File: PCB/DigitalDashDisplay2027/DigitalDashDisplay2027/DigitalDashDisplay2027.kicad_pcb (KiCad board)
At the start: 2 copper layers, 100 x 56.3 mm, 13 parts, among them IC1 LMR51430YDDCR, J1 Adafruit CAN Pal, J2 53375-0810, U1 Teensy4.0

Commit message: Began restructuring dash PCB, migrated footprints & symbols to the central library
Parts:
- removed J1: Adafruit CAN Pal, CFR 2025 Digital Dash Lib:1X07_ROUND_70
- C6: moved to F.Cu
- moved J2 13.2 mm to (175.9, 109.0)
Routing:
- net /CanLo: track 50.7 -> 0.00 mm
- net /CanHi: track 43.1 -> 0.00 mm
- net +BATT: track 16.9 -> 14.1 mm

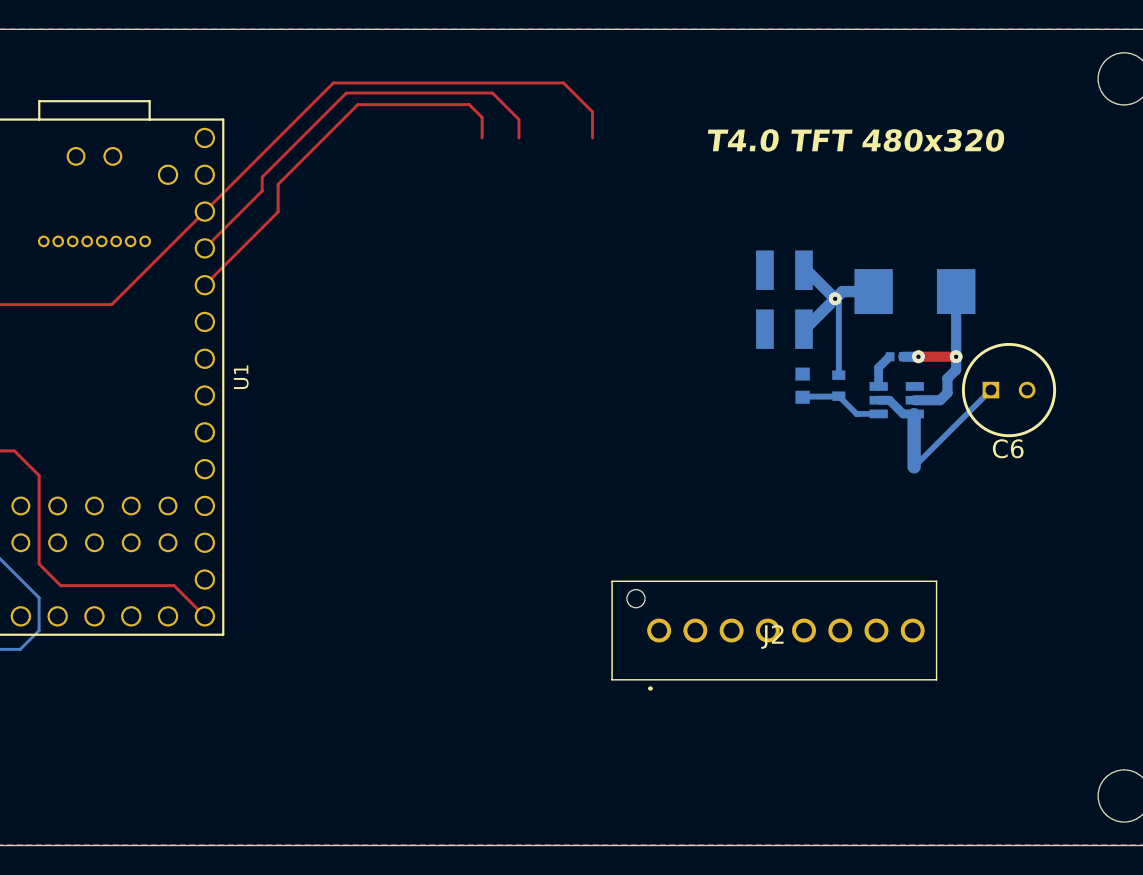
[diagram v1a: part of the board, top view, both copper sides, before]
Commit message: Began redesigning dashboard, changed multi-power rail to single power rail, rerouted buck converter
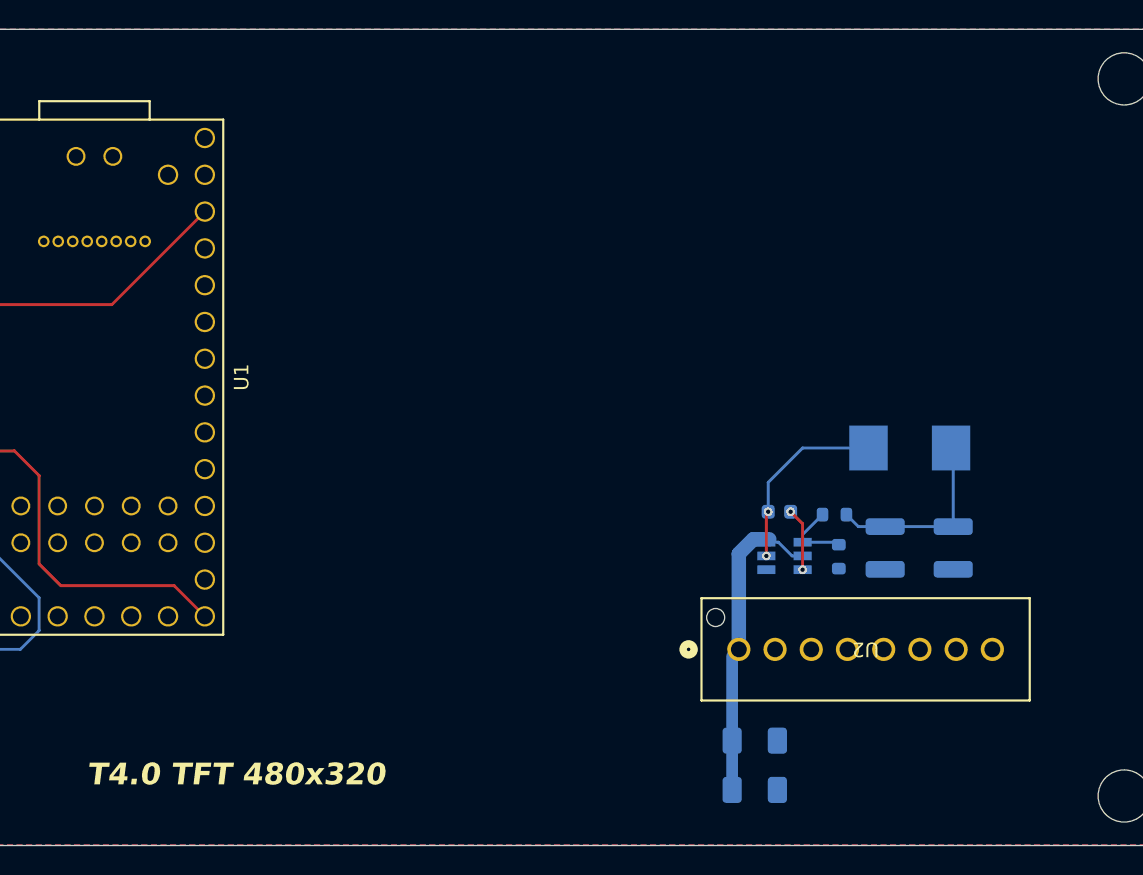
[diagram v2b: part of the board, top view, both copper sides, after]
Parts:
- removed C6: RPA0609101M025B, buck_footprints:CAPPRD250W55D630H1050
- removed C7, C8: CL32A226KOJNNNE, buck_footprints:CAPC3225X270N
- removed IC1: LMR51430YDDCR, buck_footprints:SOT95P280X110-6N
- removed J2: 53375-0810, SamacSys_Parts:533750810
- removed L5: PA4341.682ANLT, buck_footprints:INDPM7166X300N
- removed R6: ERA-3AED104V, buck_footprints:ERA3AEB101V
- removed R7: ERJ-3EKF1372V, buck_footprints:RESC1608X55N
- added C1: CC0603KRX7R7BB104, Capacitor_SMD:C_0603_1608Metric, B.Cu at (184.2, 100.8)
- added C2: C3216X5R1E476M160AC, Capacitor_SMD:C_1206_3216Metric_Pad1.33x1.80mm_HandSolder, B.Cu at (182.5, 120.0)
- added C3: CL32A226KOJNNNE, Capacitor_SMD:C_1210_3225Metric, B.Cu at (191.5, 103.3)
- added C4: CL32A226KOJNNNE, Capacitor_SMD:C_1210_3225Metric, B.Cu at (196.2, 103.3)
- added IC2: LMR51430YDDCR, CFR Library:SOT95P280X110-6N, B.Cu at (184.6, 103.8)
- added L1: PA4341.682ANLT, CFR Library:INDPM7166X300N, B.Cu at (193.2, 96.4)
- added R1: ERA-3AED104V, Resistor_SMD:R_0603_1608Metric, B.Cu at (188.0, 101.0)
- added R2: ERJ-3EKF1372V, Resistor_SMD:R_0603_1608Metric, B.Cu at (188.3, 103.9)
- added U2: ~, CFR Library:CONN08_533750810_MOL, F.Cu at (181.4, 110.3)
- C5: value CL05B104KO5NNNC -> C3216X5R1E476M160AC; footprint buck_footprints:CAPC1005X55N -> Capacitor_SMD:C_1206_3216Metric_Pad1.33x1.80mm_HandSolder
- moved C5 28.3 mm to (182.5, 116.6), turned to 180 degrees
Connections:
- C5 pad 1: Net-(IC1-CB) -> GNDREF
- C5 pad 2: Net-(IC1-SW) -> +BATT
- U1 pad 21: Net-(U1-14_A0_TX3_SPDIF_OUT) -> unconnected-(U1-14_A0_TX3_SPDIF_OUT-Pad21)
- U1 pad 22: Net-(U1-15_A1_RX3_SPDIF_IN) -> unconnected-(U1-15_A1_RX3_SPDIF_IN-Pad22)
- U1 pad 25: Net-(U1-18_A4_SDA0) -> unconnected-(U1-18_A4_SDA0-Pad25)
- U1 pad 26: Net-(U1-19_A5_SCL0) -> unconnected-(U1-19_A5_SCL0-Pad26)
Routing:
- net +3.3V: track 93.5 -> 60.5 mm
- net /CRX: track 28.8 -> 0.08 mm
- net /CTX: track 27.2 -> 0.00 mm
- net Net-(IC1-SW): track 13.4 -> 0.00 mm, vias 2 -> 0
- net Net-(IC2-SW): track 0.00 -> 13.0 mm, vias 0 -> 2
- net +BATT: track 14.1 -> 21.9 mm
- net Net-(IC1-FB): track 5.77 -> 0.00 mm
- net Net-(IC2-FB): track 0.00 -> 5.04 mm
- net Net-(IC2-CB): track 0.00 -> 4.34 mm, vias 0 -> 2
- net Net-(IC1-CB): track 2.41 -> 0.00 mm
- net +5V: track 14.2 -> 13.2 mm, vias 1 -> 0
- added copper zone on F.Cu, net GNDREF
- removed copper zone on F.Cu, net +5V
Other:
- board text added: "Buck traces need to be properly sized"

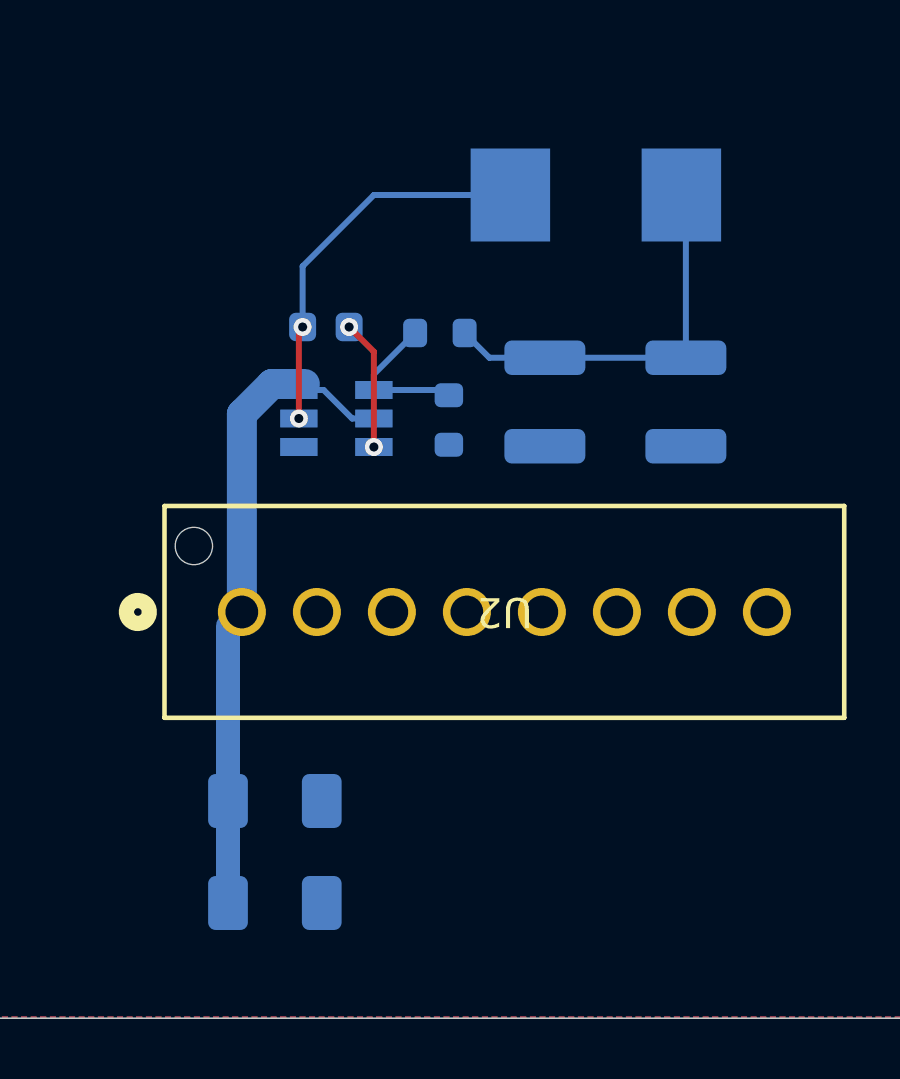
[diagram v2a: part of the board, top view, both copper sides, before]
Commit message: Sized buck converter traces, began re-routing DAQ board
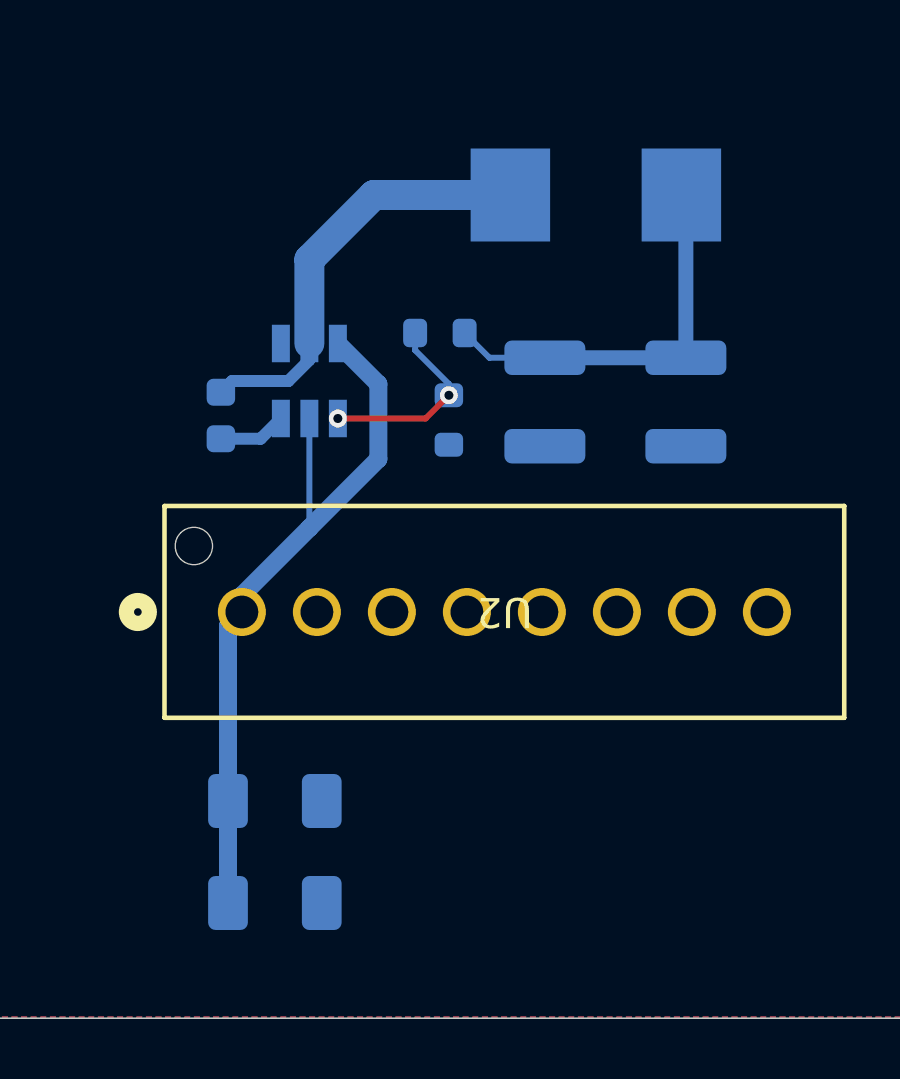
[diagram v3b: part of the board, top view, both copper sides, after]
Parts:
- moved C1 4.58 mm to (180.7, 103.8), turned to 90 degrees
- moved IC2 1.54 mm to (183.7, 102.6), turned to -90 degrees
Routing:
- net +BATT: track 21.9 -> 24.9 mm
- net Net-(IC2-CB): track 4.34 -> 2.28 mm, vias 2 -> 0
- net Net-(IC2-FB): track 5.04 -> 6.81 mm, vias 0 -> 2
- net Net-(IC2-SW): track 13.0 -> 14.3 mm, vias 2 -> 0
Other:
- board text removed: "Buck traces need to be properly sized"
